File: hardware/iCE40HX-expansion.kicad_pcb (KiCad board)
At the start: 2 copper layers, 55 parts, among them J1 EXT3, J2 EXT1, J3 AudioJack3_Ground, J4 Conn_01x34, J5 AudioJack3_Ground, J6 Conn_01x04, J7 Conn_01x06, U1 ADV7180BCP32Z-RL, U2 AMS1117-1.8, Y1 28.63636MHz

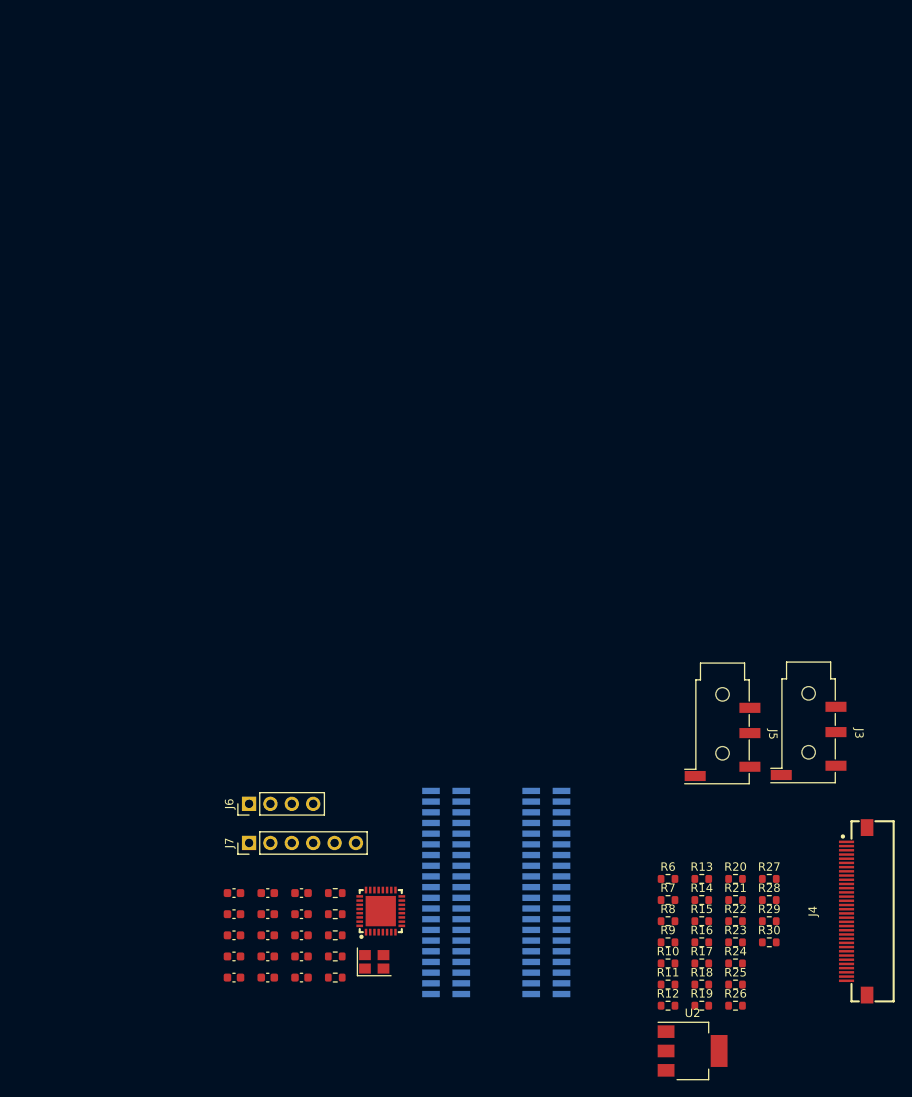
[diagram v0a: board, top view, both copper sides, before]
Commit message: moved R2R dacs into hierarchical sheets
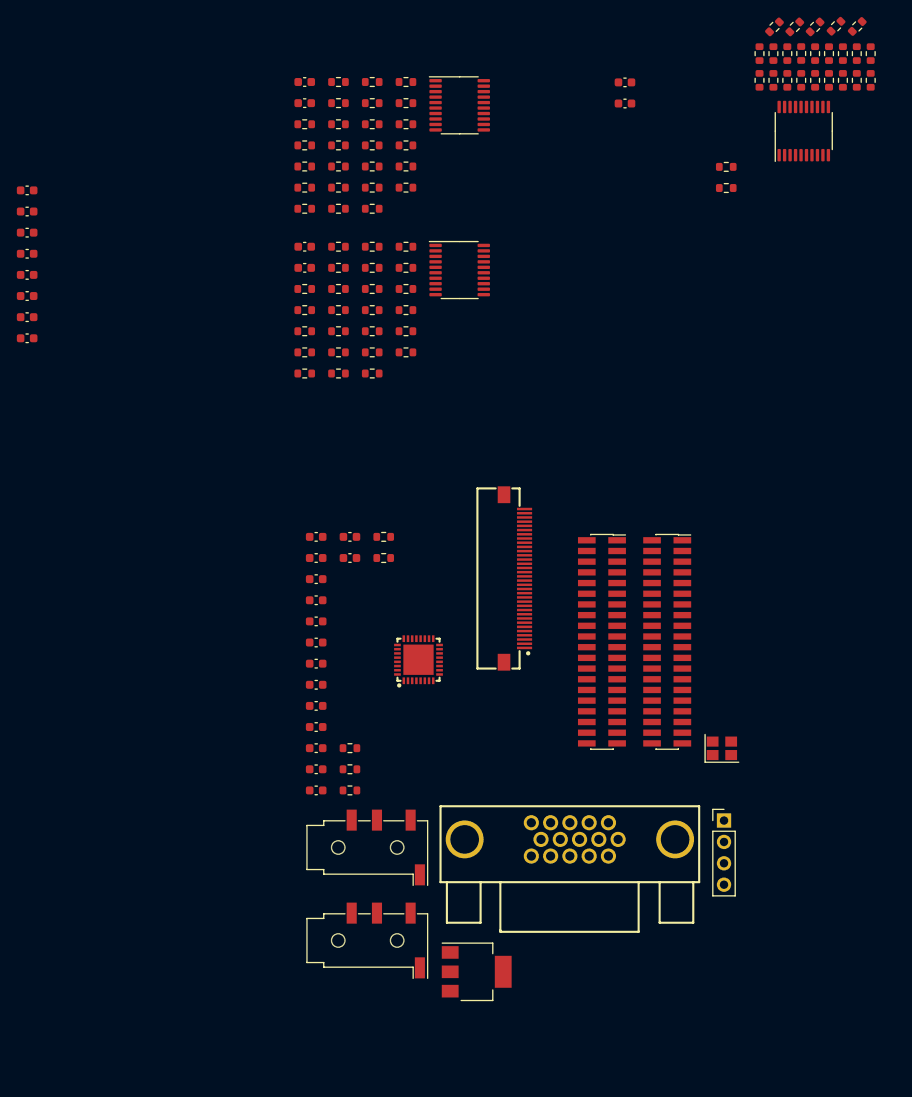
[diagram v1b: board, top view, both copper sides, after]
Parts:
- removed J7: Conn_01x06, Connector_PinHeader_2.54mm:PinHeader_1x06_P2.54mm_Vertical
- added C16: 0.1uf, Capacitor_SMD:C_0603_1608Metric, F.Cu at (57.6, -3.35)
- added C16: 0.1uf, Capacitor_SMD:C_0603_1608Metric, F.Cu at (24.6, -10.0)
- added C17: 10nf, Capacitor_SMD:C_0603_1608Metric, F.Cu at (57.6, -0.84)
- added C17: 10nf, Capacitor_SMD:C_0603_1608Metric, F.Cu at (24.6, -7.53)
- added C18: 0.1uf, Capacitor_SMD:C_0603_1608Metric, F.Cu at (57.6, -22.9)
- added C18: 0.1uf, Capacitor_SMD:C_0603_1608Metric, F.Cu at (24.6, -5.02)
- added C19: 10nf, Capacitor_SMD:C_0603_1608Metric, F.Cu at (57.6, -20.4)
- added C19: 10nf, Capacitor_SMD:C_0603_1608Metric, F.Cu at (24.6, -2.51)
- added C20: 0.1uf, Capacitor_SMD:C_0603_1608Metric, F.Cu at (95.7, -22.9)
- added C20: 0.1uf, Capacitor_SMD:C_0603_1608Metric, F.Cu at (24.6, 0.00)
- added C21: 10nf, Capacitor_SMD:C_0603_1608Metric, F.Cu at (24.6, 2.51)
- added C21: 10nf, Capacitor_SMD:C_0603_1608Metric, F.Cu at (95.7, -20.4)
- added C22: 10uf, Capacitor_SMD:C_0603_1608Metric, F.Cu at (24.6, 5.02)
- added C23: 10uf, Capacitor_SMD:C_0603_1608Metric, F.Cu at (24.6, 7.53)
- added J8: DE15_Plug_HighDensity, C711364:DSUB-TH_HYC06-HDR15B-060, F.Cu at (89.1, 67.1)
- added R100: 270, Resistor_SMD:R_0603_1608Metric, F.Cu at (69.6, -3.35)
- added R101: 270, Resistor_SMD:R_0603_1608Metric, F.Cu at (69.6, -0.84)
- added R102: 270, Resistor_SMD:R_0603_1608Metric, F.Cu at (69.6, 1.67)
- added R103: 270, Resistor_SMD:R_0603_1608Metric, F.Cu at (69.6, 4.18)
- added R104: 270, Resistor_SMD:R_0603_1608Metric, F.Cu at (69.6, 6.69)
- added R105: 270, Resistor_SMD:R_0603_1608Metric, F.Cu at (69.6, 9.20)
- added R31: 270, Resistor_SMD:R_0603_1608Metric, F.Cu at (111.6, -23.1)
- added R32: 270, Resistor_SMD:R_0603_1608Metric, F.Cu at (113.3, -23.1)
- added R33: 270, Resistor_SMD:R_0603_1608Metric, F.Cu at (114.9, -23.1)
- added R34: 270, Resistor_SMD:R_0603_1608Metric, F.Cu at (116.6, -23.1)
- added R35: 270, Resistor_SMD:R_0603_1608Metric, F.Cu at (118.2, -23.1)
- added R36: 270, Resistor_SMD:R_0603_1608Metric, F.Cu at (119.9, -23.1)
- added R37: 270, Resistor_SMD:R_0603_1608Metric, F.Cu at (123.2, -23.1)
- added R38: 270, Resistor_SMD:R_0603_1608Metric, F.Cu at (121.5, -23.1)
- added R39: 270, Resistor_SMD:R_0603_1608Metric, F.Cu at (124.8, -23.1)
- added R40: 270, Resistor_SMD:R_0603_1608Metric, F.Cu at (111.6, -26.3)
- added R41: 270, Resistor_SMD:R_0603_1608Metric, F.Cu at (113.3, -26.3)
- added R42: 270, Resistor_SMD:R_0603_1608Metric, F.Cu at (114.9, -26.3)
- added R43: 270, Resistor_SMD:R_0603_1608Metric, F.Cu at (116.6, -26.3)
- added R44: 270, Resistor_SMD:R_0603_1608Metric, F.Cu at (118.2, -26.3)
- added R45: 270, Resistor_SMD:R_0603_1608Metric, F.Cu at (119.9, -26.3)
- added R46: 270, Resistor_SMD:R_0603_1608Metric, F.Cu at (123.2, -26.3)
- added R47: 270, Resistor_SMD:R_0603_1608Metric, F.Cu at (121.5, -26.3)
- added R48: 270, Resistor_SMD:R_0603_1608Metric, F.Cu at (124.8, -26.3)
- added R49: 270, Resistor_SMD:R_0603_1608Metric, F.Cu at (113.4, -29.5)
- added R50: 270, Resistor_SMD:R_0603_1608Metric, F.Cu at (115.8, -29.5)
- added R51: 270, Resistor_SMD:R_0603_1608Metric, F.Cu at (118.2, -29.5)
- added R52: 270, Resistor_SMD:R_0603_1608Metric, F.Cu at (120.7, -29.5)
- added R53: 270, Resistor_SMD:R_0603_1608Metric, F.Cu at (123.2, -29.5)
- added R54: 270, Resistor_SMD:R_0603_1608Metric, F.Cu at (107.7, -12.8)
- added R55: 270, Resistor_SMD:R_0603_1608Metric, F.Cu at (107.7, -10.3)
- added R81: 270, Resistor_SMD:R_0603_1608Metric, F.Cu at (57.6, 1.67)
- added R82: 270, Resistor_SMD:R_0603_1608Metric, F.Cu at (57.6, 4.18)
- added R83: 270, Resistor_SMD:R_0603_1608Metric, F.Cu at (57.6, 6.69)
- added R84: 270, Resistor_SMD:R_0603_1608Metric, F.Cu at (57.6, 9.20)
- added R85: 270, Resistor_SMD:R_0603_1608Metric, F.Cu at (57.6, 11.7)
- added R86: 270, Resistor_SMD:R_0603_1608Metric, F.Cu at (61.6, -3.35)
- added R87: 270, Resistor_SMD:R_0603_1608Metric, F.Cu at (61.6, -0.84)
- added R88: 270, Resistor_SMD:R_0603_1608Metric, F.Cu at (61.6, 1.67)
- added R89: 270, Resistor_SMD:R_0603_1608Metric, F.Cu at (61.6, 4.18)
- added R90: 270, Resistor_SMD:R_0603_1608Metric, F.Cu at (61.6, 6.69)
- added R91: 270, Resistor_SMD:R_0603_1608Metric, F.Cu at (61.6, 9.20)
- added R92: 270, Resistor_SMD:R_0603_1608Metric, F.Cu at (61.6, 11.7)
- added R93: 270, Resistor_SMD:R_0603_1608Metric, F.Cu at (65.6, -3.35)
- added R94: 270, Resistor_SMD:R_0603_1608Metric, F.Cu at (65.6, -0.84)
- added R95: 270, Resistor_SMD:R_0603_1608Metric, F.Cu at (65.6, 1.67)
- added R96: 270, Resistor_SMD:R_0603_1608Metric, F.Cu at (65.6, 4.18)
- added R97: 270, Resistor_SMD:R_0603_1608Metric, F.Cu at (65.6, 6.69)
- added R98: 270, Resistor_SMD:R_0603_1608Metric, F.Cu at (65.6, 9.20)
- added R99: 270, Resistor_SMD:R_0603_1608Metric, F.Cu at (65.6, 11.7)
- added U3: 74LVC245A, Package_SO:TSSOP-20_4.4x6.5mm_P0.65mm, F.Cu at (76.0, -20.1)
- added U4: 74LVC245A, Package_SO:TSSOP-20_4.4x6.5mm_P0.65mm, F.Cu at (116.9, -17.1)
- added U6: 74LVC245A, Package_SO:TSSOP-20_4.4x6.5mm_P0.65mm, F.Cu at (76.0, -0.58)
- J1, J2: moved to F.Cu
- R10, R11, R12, R13, R14, R15, R16, R17, R18, R19, R20, R21, R22, R23, R24, R25, R26, R27, R28, R29, R30, R6, R7, R8, R9: value 470 -> 270
- moved R11 114.2 mm to (61.6, -22.9)
- moved R12 114.2 mm to (61.6, -20.4)
- moved R18 114.2 mm to (65.6, -22.9)
- moved R19 114.2 mm to (65.6, -20.4)
- moved R25 114.2 mm to (69.6, -22.9)
- moved R26 114.2 mm to (69.6, -20.4)
- moved R10 99.5 mm to (57.6, -7.86)
- moved R14 99.5 mm to (61.6, -15.4)
- moved R17 99.5 mm to (61.6, -7.86)
- moved R21 99.5 mm to (65.6, -15.4)
- moved R24 99.5 mm to (65.6, -7.86)
- moved R28 99.5 mm to (69.6, -15.4)
- moved R7 99.5 mm to (57.6, -15.4)
- moved R13 99.5 mm to (61.6, -17.9)
- moved R15 99.5 mm to (61.6, -12.9)
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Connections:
- net /RGB_CLK renamed /CLK
- net /RGB_EN renamed /EN
- J4 pad 10: /RGB_B4 -> /PIO0_19
- J4 pad 11: /RGB_B5 -> /PIO0_18
- J4 pad 12: /RGB_B6 -> /PIO0_17
- J4 pad 13: /RGB_B7 -> /PIO0_16
- J4 pad 14: /RGB_G0 -> /PIO0_15
- J4 pad 15: /RGB_G1 -> /PIO0_14
- J4 pad 16: /RGB_G2 -> /PIO0_13
- J4 pad 17: /RGB_G3 -> /PIO0_12
- J4 pad 18: /RGB_G4 -> /PIO0_11
- J4 pad 19: /RGB_G5 -> /PIO0_10
- J4 pad 20: /RGB_G6 -> /PIO0_09
- J4 pad 21: /RGB_G7 -> /PIO0_08
- J4 pad 22: /RGB_R0 -> /PIO0_07
- J4 pad 23: /RGB_R1 -> /PIO0_06
- J4 pad 24: /RGB_R2 -> /PIO0_05
- J4 pad 25: /RGB_R3 -> /PIO0_04
- J4 pad 26: /RGB_R4 -> /PIO0_03
- J4 pad 27: /RGB_R5 -> /PIO0_02
- J4 pad 28: /RGB_R6 -> /PIO0_01
- J4 pad 29: /RGB_R7 -> /PIO0_00
- J4 pad 3: /RGB_HSYNC -> /HSYNC
- J4 pad 5: /RGB_VSYNC -> /VSYNC
- J4 pad 6: /RGB_B0 -> /PIO0_23
- J4 pad 7: /RGB_B1 -> /PIO0_22
- J4 pad 8: /RGB_B2 -> /PIO0_21
- J4 pad 9: /RGB_B3 -> /PIO0_20
- R10 pad 1: Net-(R10-Pad1) -> Net-(U3-B3)
- R10 pad 2: /PIO0_04 -> Net-(R10-Pad2)
- R11 pad 1: Net-(R11-Pad1) -> Net-(U3-B4)
- R11 pad 2: /PIO0_05 -> Net-(R11-Pad2)
- R12 pad 1: Net-(R12-Pad1) -> Net-(U3-B5)
- R12 pad 2: /PIO0_06 -> Net-(R12-Pad2)
- R13 pad 1: Net-(R13-Pad1) -> Net-(U3-B6)
- R13 pad 2: /PIO0_07 -> Net-(R13-Pad2)
- R14 pad 1: Net-(R14-Pad1) -> Net-(U3-B7)
- R16 pad 2: Net-(R16-Pad2) -> Net-(R15-Pad2)
- R18 pad 2: Net-(R10-Pad1) -> Net-(R18-Pad2)
- R19 pad 1: Net-(R19-Pad1) -> Net-(R10-Pad2)
- R19 pad 2: Net-(R11-Pad1) -> Net-(R19-Pad2)
- R20 pad 1: Net-(R20-Pad1) -> Net-(R11-Pad2)
- R20 pad 2: Net-(R12-Pad1) -> Net-(R20-Pad2)
- R21 pad 1: Net-(R21-Pad1) -> Net-(R12-Pad2)
- R21 pad 2: Net-(R13-Pad1) -> Net-(R21-Pad2)
- R22 pad 1: Net-(R15-Pad1) -> Net-(R13-Pad2)
- R22 pad 2: Net-(R14-Pad1) -> Net-(R22-Pad2)
- R23 pad 1: Net-(R16-Pad1) -> Net-(R14-Pad2)
- R23 pad 2: Net-(R15-Pad1) -> /GREEN
- R24 pad 1: Net-(R17-Pad1) -> Net-(R17-Pad2)
- R24 pad 2: Net-(R16-Pad1) -> Net-(R15-Pad2)
- R25 pad 1: Net-(R18-Pad1) -> Net-(R18-Pad2)
- R25 pad 2: Net-(R17-Pad1) -> Net-(R17-Pad2)
- R26 pad 1: Net-(R19-Pad1) -> Net-(R19-Pad2)
- R26 pad 2: Net-(R18-Pad1) -> Net-(R18-Pad2)
- R27 pad 1: Net-(R20-Pad1) -> Net-(R20-Pad2)
- R27 pad 2: Net-(R19-Pad1) -> Net-(R19-Pad2)
- R28 pad 1: Net-(R21-Pad1) -> Net-(R21-Pad2)
- R28 pad 2: Net-(R20-Pad1) -> Net-(R20-Pad2)
- R29 pad 1: Net-(R14-Pad1) -> Net-(R22-Pad2)
- R29 pad 2: Net-(R29-Pad2) -> Net-(R21-Pad2)
- R30 pad 1: Net-(R29-Pad2) -> /GREEN
- R30 pad 2: GND -> Net-(R22-Pad2)
- R6 pad 1: Net-(R14-Pad2) -> GND
- R6 pad 2: /PIO0_00 -> Net-(R15-Pad1)
- R7 pad 1: Net-(R15-Pad2) -> Net-(U3-B0)
- R7 pad 2: /PIO0_01 -> Net-(R16-Pad1)
- R8 pad 1: Net-(R16-Pad2) -> Net-(U3-B1)
- R8 pad 2: /PIO0_02 -> Net-(R17-Pad1)
- R9 pad 1: Net-(R17-Pad2) -> Net-(U3-B2)
- R9 pad 2: /PIO0_03 -> Net-(R18-Pad1)
- U1 pad 10: unconnected-(U1-P2-Pad10) -> /PIO1_16
- U1 pad 15: unconnected-(U1-P1-Pad15) -> /PIO1_15
- U1 pad 16: unconnected-(U1-P0-Pad16) -> /PIO1_14
- U1 pad 5: unconnected-(U1-P7-Pad5) -> /PIO1_21
- U1 pad 6: unconnected-(U1-P6-Pad6) -> /PIO1_20
- U1 pad 7: unconnected-(U1-P5-Pad7) -> /PIO1_19
- U1 pad 8: unconnected-(U1-P4-Pad8) -> /PIO1_18
- U1 pad 9: unconnected-(U1-P3-Pad9) -> /PIO1_17
